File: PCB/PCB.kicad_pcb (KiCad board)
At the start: 2 copper layers, 266.7 x 81.4 mm, 125 parts, among them J1 USB-C USB 2.0 MC-372, J2 Conn_01x04, J3 Conn_01x02, Q1 AO3407, Q2 AO3406, SW1 SW_Push, SW10 SW_Push, SW11 SW_Push, SW12 SW_Push, SW13 SW_Push, SW14 SW_Push, SW15 SW_Push, SW16 SW_Push, SW17 SW_Push, SW18 SW_Push, SW19 SW_Push, SW2 SW_Push, SW20 SW_Push, SW21 SW_Push, SW22 SW_Push, SW23 SW_Push, SW24 SW_Push, SW25 SW_Push, SW26 SW_Push, SW27 SW_Push, SW28 SW_Push, SW29 SW_Push, SW3 SW_Push, SW30 SW_Push, SW31 SW_Push, SW32 SW_Push, SW33 SW_Push, SW34 SW_Push, SW35 SW_Push, SW36 SW_Push, SW37 SW_Push, SW38 SW_Push, SW39 SW_Push, SW4 SW_Push, SW40 SW_Push, SW41 SW_Push, SW42 SW_Push, SW43 SW_Push, SW44 SW_Push, SW45 SW_Push, SW46 SW_Push, SW47 SW_Push, SW48 SW_Push, SW49 SW_Push, SW5 SW_Push, SW50 SW_Push, SW51 MSK-12C02, SW6 SW_Push, SW7 SW_Push, SW8 SW_Push, SW9 SW_Push, U1 E73-2G4M08S1C, U2 MCP73831, U3 AP2112K-3.3

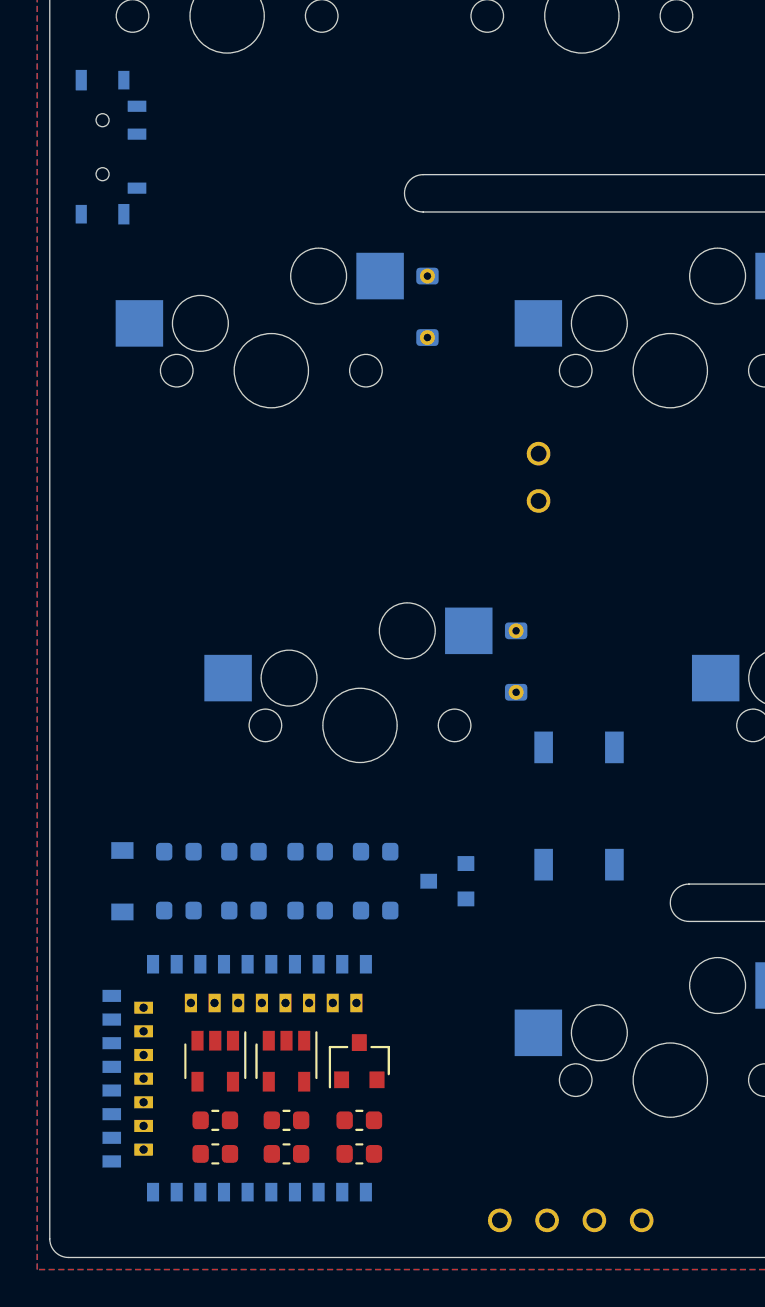
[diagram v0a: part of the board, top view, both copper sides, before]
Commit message: Move components for better routing
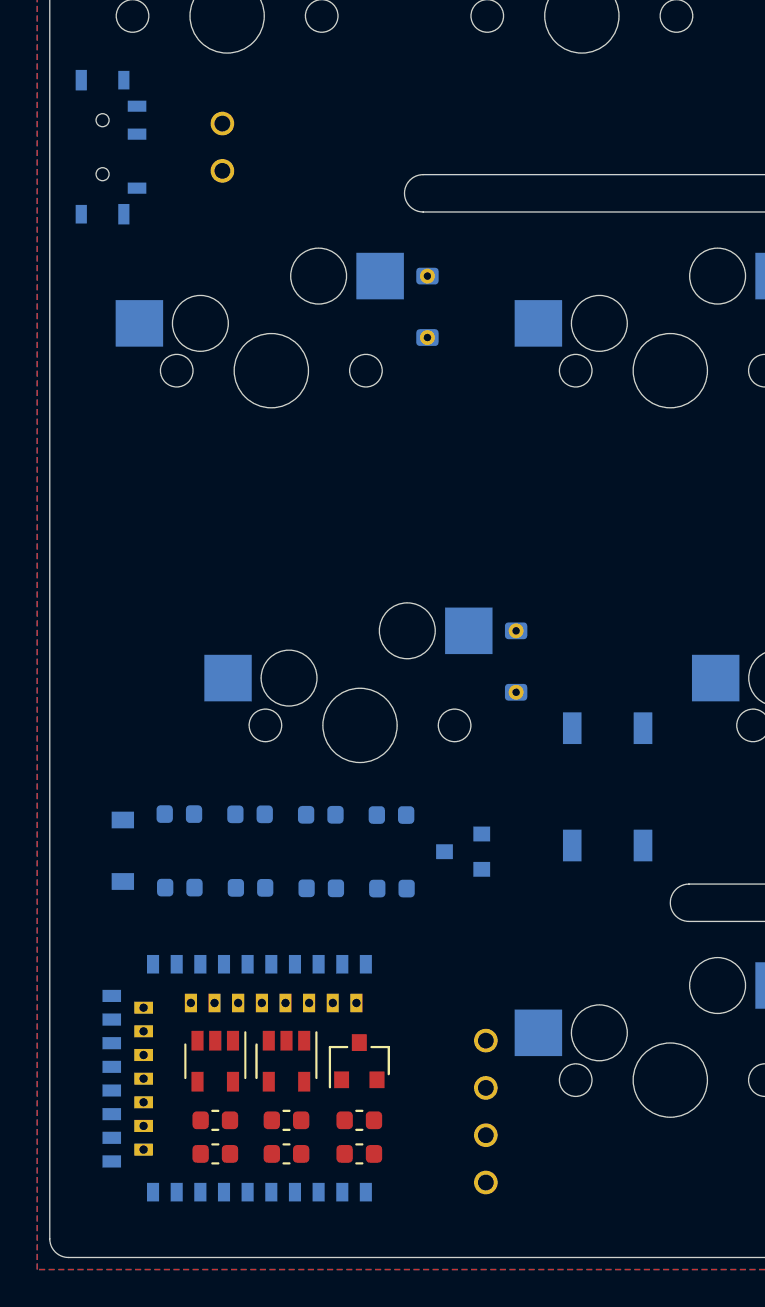
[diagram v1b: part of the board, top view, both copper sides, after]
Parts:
- moved J3 24.5 mm to (23.9, 57.8), turned to 90 degrees
- moved J2 7.41 mm to (38.0, 109.6), turned to 90 degrees
- moved R7 2.14 mm to (33.0, 93.7)
- moved R5 2.06 mm to (29.2, 93.7)
- moved D49 2.03 mm to (25.4, 93.7)
- moved R1 2.02 mm to (21.6, 93.7)
- moved SW50 1.85 mm to (44.6, 92.2)
- moved Q2 1.80 mm to (36.8, 95.7)
- moved D51 1.64 mm to (18.5, 95.6)
- moved R4 1.47 mm to (33.0, 97.7)
- moved R2 1.33 mm to (29.2, 97.7)
- moved D50 1.27 mm to (25.4, 97.6)
- moved R6 1.23 mm to (21.6, 97.6)
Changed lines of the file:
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@@
     (solder_mask_min_width 0.25)
     (aux_axis_origin 0 0)
-    (visible_elements 7FFFFFFF)
+    (visible_elements 7FFFF7FF)
     (pcbplotparams
       (layerselection 0x010fc_ffffffff)
@@
   )
   (module nrfmicro:connector_swd (layer F.Cu)
-    (at 42.5831 115.481)
-    (fp_text reference J2 (at 0 -3.175) (layer F.Fab) hide
+    (at 38.0237 109.6391 90)
+    (fp_text reference J2 (at 0 -3.175 90) (layer F.Fab) hide
       (effects (font (size 1 1) (thickness 0.15)))
     )
-    (fp_text value Conn_01x04 (at 0 -5.08) (layer F.Fab) hide
+    (fp_text value Conn_01x04 (at 0 -5.08 90) (layer F.Fab) hide
       (effects (font (size 1 1) (thickness 0.15)))
     )
-    (fp_text user SWD (at -1.27 -1.27) (layer F.SilkS) hide
+    (fp_text user SWD (at -1.27 -1.27 90) (layer F.SilkS) hide
       (effects (font (size 0.7 0.7) (thickness 0.15)))
     )
-    (fp_text user SWC (at 1.27 -1.27 180) (layer F.SilkS) hide
+    (fp_text user SWC (at 1.27 -1.27 270) (layer F.SilkS) hide
       (effects (font (size 0.7 0.7) (thickness 0.15)))
     )
-    (fp_text user GND (at 3.81 -1.27) (layer F.SilkS) hide
+    (fp_text user GND (at 3.81 -1.27 90) (layer F.SilkS) hide
       (effects (font (size 0.7 0.7) (thickness 0.15)))
     )
-    (fp_text user VCC (at 1.27 -1.27) (layer F.SilkS) hide
+    (fp_text user VCC (at 1.27 -1.27 90) (layer F.SilkS) hide
       (effects (font (size 0.7 0.7) (thickness 0.15)))
     )
-    (pad 4 thru_hole circle (at 3.81 0) (size 1.27 1.27) (drill 0.85) (layers *.Cu *.Mask)
+    (pad 4 thru_hole circle (at 3.81 0 90) (size 1.27 1.27) (drill 0.85) (layers *.Cu *.Mask)
       (net 1 GND))
-    (pad 3 thru_hole circle (at 1.27 0) (size 1.27 1.27) (drill 0.85) (layers *.Cu *.Mask)
+    (pad 3 thru_hole circle (at 1.27 0 90) (size 1.27 1.27) (drill 0.85) (layers *.Cu *.Mask)
       (net 4 VCC))
-    (pad 1 thru_hole circle (at -3.81 0 90) (size 1.27 1.27) (drill 0.85) (layers *.Cu *.Mask)
+    (pad 1 thru_hole circle (at -3.81 0 180) (size 1.27 1.27) (drill 0.85) (layers *.Cu *.Mask)
       (net 68 SWC))
-    (pad 2 thru_hole circle (at -1.27 0) (size 1.27 1.27) (drill 0.85) (layers *.Cu *.Mask)
+    (pad 2 thru_hole circle (at -1.27 0 90) (size 1.27 1.27) (drill 0.85) (layers *.Cu *.Mask)
       (net 69 SWD))
   )
   (module nrfmicro:connectro_bat (layer B.Cu)
-    (at 40.8559 75.5777 270)
+    (at 23.876 57.8485 90)
     (fp_text reference J3 (at 0 -1.7145 270) (layer Dwgs.User) hide
       (effects (font (size 1 1) (thickness 0.15)))
@@
       (effects (font (size 0.7 0.7) (thickness 0.15)) (justify mirror))
     )
-    (pad 2 thru_hole circle (at 1.27 0 270) (size 1.27 1.27) (drill 0.85) (layers *.Cu *.Mask)
+    (pad 2 thru_hole circle (at 1.27 0 90) (size 1.27 1.27) (drill 0.85) (layers *.Cu *.Mask)
       (net 1 GND))
-    (pad 1 thru_hole circle (at -1.27 0 270) (size 1.27 1.27) (drill 0.85) (layers *.Cu *.Mask)
+    (pad 1 thru_hole circle (at -1.27 0 90) (size 1.27 1.27) (drill 0.85) (layers *.Cu *.Mask)
       (net 2 VBAT))
   )
@@
   )
   (module Keebio-Parts:SW_SPST_TL3342 (layer B.Cu)
-    (at 43.0276 93.2307 270)
+    (at 44.5643 92.202 270)
     (descr "Low-profile SMD Tactile Switch, https://www.e-switch.com/system/asset/product_line/data_sheet/165/TL3342.pdf")
     (tags "SPST Tactile Switch")
@@
   )
   (module Resistor_SMD:R_0603_1608Metric (layer B.Cu)
-    (at 32.1056 95.6818)
+    (at 32.9565 93.7133)
     (descr "Resistor SMD 0603 (1608 Metric), square (rectangular) end terminal, IPC_7351 nominal, (Body size source: http://www.tortai-tech.com/upload/download/2011102023233369053.pdf), generated with kicad-footprint-generator")
     (tags resistor)
@@
   )
   (module Resistor_SMD:R_0603_1608Metric (layer B.Cu)
-    (at 21.5392 98.8441 180)
+    (at 21.59 97.6122 180)
     (descr "Resistor SMD 0603 (1608 Metric), square (rectangular) end terminal, IPC_7351 nominal, (Body size source: http://www.tortai-tech.com/upload/download/2011102023233369053.pdf), generated with kicad-footprint-generator")
     (tags resistor)
@@
   )
   (module Resistor_SMD:R_0603_1608Metric (layer B.Cu)
-    (at 28.5877 95.6818)
+    (at 29.1592 93.7006)
     (descr "Resistor SMD 0603 (1608 Metric), square (rectangular) end terminal, IPC_7351 nominal, (Body size source: http://www.tortai-tech.com/upload/download/2011102023233369053.pdf), generated with kicad-footprint-generator")
     (tags resistor)
@@
   )
   (module Resistor_SMD:R_0603_1608Metric (layer B.Cu)
-    (at 32.1056 98.8441 180)
+    (at 32.9819 97.663 180)
     (descr "Resistor SMD 0603 (1608 Metric), square (rectangular) end terminal, IPC_7351 nominal, (Body size source: http://www.tortai-tech.com/upload/download/2011102023233369053.pdf), generated with kicad-footprint-generator")
     (tags resistor)
@@
   )
   (module Resistor_SMD:R_0603_1608Metric (layer B.Cu)
-    (at 28.5877 98.8441)
+    (at 29.1846 97.6503)
     (descr "Resistor SMD 0603 (1608 Metric), square (rectangular) end terminal, IPC_7351 nominal, (Body size source: http://www.tortai-tech.com/upload/download/2011102023233369053.pdf), generated with kicad-footprint-generator")
     (tags resistor)
@@
   )
   (module Resistor_SMD:R_0603_1608Metric (layer B.Cu)
-    (at 21.5392 95.6818)
+    (at 21.5646 93.6625)
     (descr "Resistor SMD 0603 (1608 Metric), square (rectangular) end terminal, IPC_7351 nominal, (Body size source: http://www.tortai-tech.com/upload/download/2011102023233369053.pdf), generated with kicad-footprint-generator")
     (tags resistor)
@@
   )
   (module Package_TO_SOT_SMD:SOT-23 (layer B.Cu)
-    (at 35.9537 97.2693 180)
+    (at 36.8046 95.6818 180)
     (descr "SOT-23, Standard")
     (tags SOT-23)
@@
   )
   (module Diode_SMD:D_SOD-123 (layer B.Cu)
-    (at 18.5039 97.2693 90)
+    (at 18.5293 95.631 90)
     (descr SOD-123)
     (tags SOD-123)
@@
   )
   (module LED_SMD:LED_0603_1608Metric (layer B.Cu)
-    (at 25.0317 98.8441)
+    (at 25.3873 97.6249)
     (descr "LED SMD 0603 (1608 Metric), square (rectangular) end terminal, IPC_7351 nominal, (Body size source: http://www.tortai-tech.com/upload/download/2011102023233369053.pdf), generated with kicad-footprint-generator")
     (tags diode)
@@
   )
   (module LED_SMD:LED_0603_1608Metric (layer B.Cu)
-    (at 25.0317 95.6818)
+    (at 25.3619 93.6752)
     (descr "LED SMD 0603 (1608 Metric), square (rectangular) end terminal, IPC_7351 nominal, (Body size source: http://www.tortai-tech.com/upload/download/2011102023233369053.pdf), generated with kicad-footprint-generator")
     (tags diode)
@@
     )
   )
-  (gr_text SWD (at 41.3004 113.9444) (layer B.SilkS)
+  (gr_text SWD (at 36.4871 110.9218 90) (layer B.SilkS)
     (effects (font (size 0.7 0.7) (thickness 0.175)) (justify mirror))
   )
-  (gr_text SWC (at 38.7731 113.9571) (layer B.SilkS)
+  (gr_text SWC (at 36.4998 113.4491 90) (layer B.SilkS)
     (effects (font (size 0.7 0.7) (thickness 0.175)) (justify mirror))
   )
-  (gr_text "-\n" (at 46.3931 113.9444) (layer B.SilkS)
+  (gr_text "-\n" (at 36.4871 105.8291 90) (layer B.SilkS)
     (effects (font (size 0.7 0.7) (thickness 0.175)) (justify mirror))
   )
-  (gr_text + (at 43.8531 113.9444) (layer B.SilkS)
+  (gr_text + (at 36.4871 108.3691 90) (layer B.SilkS)
     (effects (font (size 0.7 0.7) (thickness 0.175)) (justify mirror))
   )

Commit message: Remove flex hole
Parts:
- removed G2: LOGO, Infinity:MechCultLogo
- removed G3: LOGO, Infinity:InfinityText
- added G***: LOGO, Infinity:InfinityText, B.Cu at (153.1, 57.8)
- moved SW50 23.1 mm to (51.3, 114.3), turned to 180 degrees
- moved J2 7.27 mm to (40.9, 116.3), turned to 0 degrees
- moved J3 1.88 mm to (22.0, 57.8)
- moved G1 0.38 mm to (269.4, 108.0)
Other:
- outline, holes or cut-outs redrawn

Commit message: Route tracks
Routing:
- net SWO: track 0.00 -> 359.3 mm, vias 0 -> 5
- net /P0.24: track 0.00 -> 355.6 mm, vias 0 -> 5
- net /P1.04: track 0.00 -> 333.2 mm, vias 0 -> 1
- net /P0.10: track 0.00 -> 327.5 mm, vias 0 -> 2
- net /P0.01: track 0.00 -> 316.6 mm, vias 0 -> 2
- net /P0.12: track 0.00 -> 309.3 mm, vias 0 -> 1
- net /P0.05: track 0.00 -> 308.4 mm, vias 0 -> 4
- net /P0.30: track 0.00 -> 300.2 mm, vias 0 -> 9
- net /P0.00: track 0.00 -> 295.2 mm, vias 0 -> 10
- net /P0.09: track 0.00 -> 293.0 mm, vias 0 -> 2
- net /P0.22: track 0.00 -> 263.2 mm, vias 0 -> 1
- net /P0.31: track 0.00 -> 232.4 mm, vias 0 -> 8
- net GND: track 0.00 -> 199.6 mm, vias 0 -> 3
- net /P0.29: track 0.00 -> 197.5 mm
- net /P1.13: track 0.00 -> 164.3 mm, vias 0 -> 4
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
